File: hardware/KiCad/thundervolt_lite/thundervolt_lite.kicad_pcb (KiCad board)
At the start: 4 copper layers, 46.9 x 54.8 mm, 59 parts, among them U1 TPS628681ARQYR, U2 TPS628681ARQYR, U3 TPS628682ARQYR, U4 TPS63810YFFR, U5 ATTINY1616-MNR, U7 TMP1075NDRLR, U8 MIC5365-1.8YC5-TR

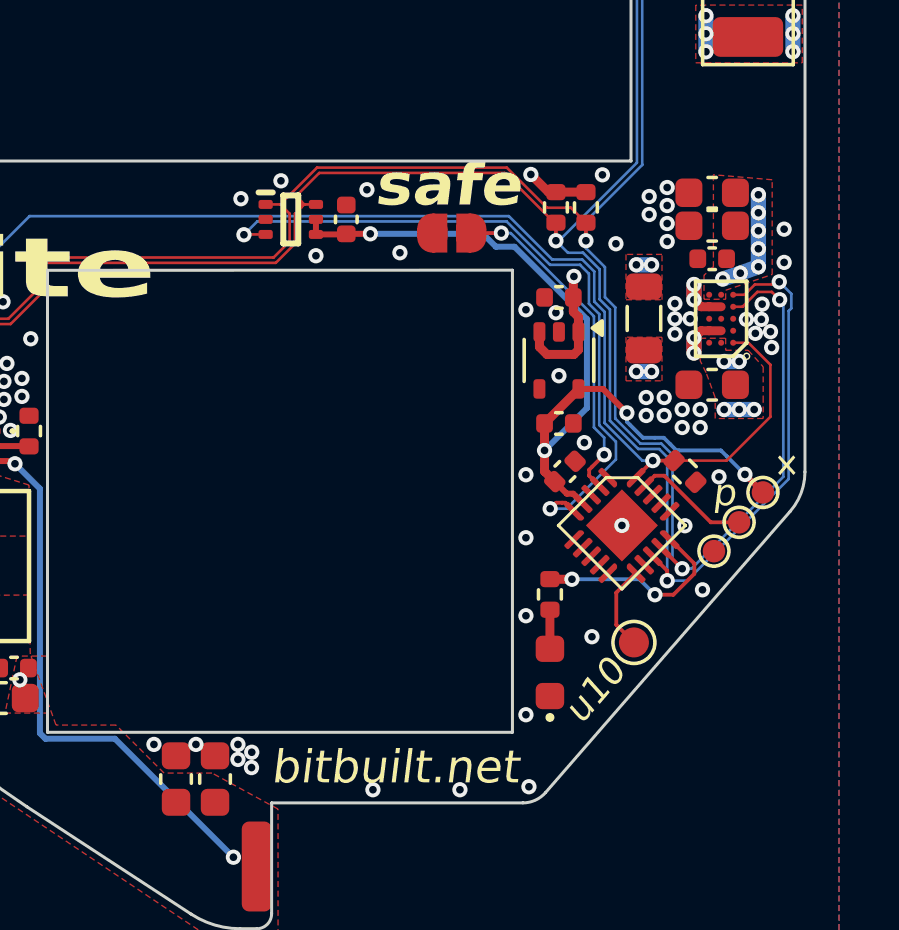
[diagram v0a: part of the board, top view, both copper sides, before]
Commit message: U10 FET Mode
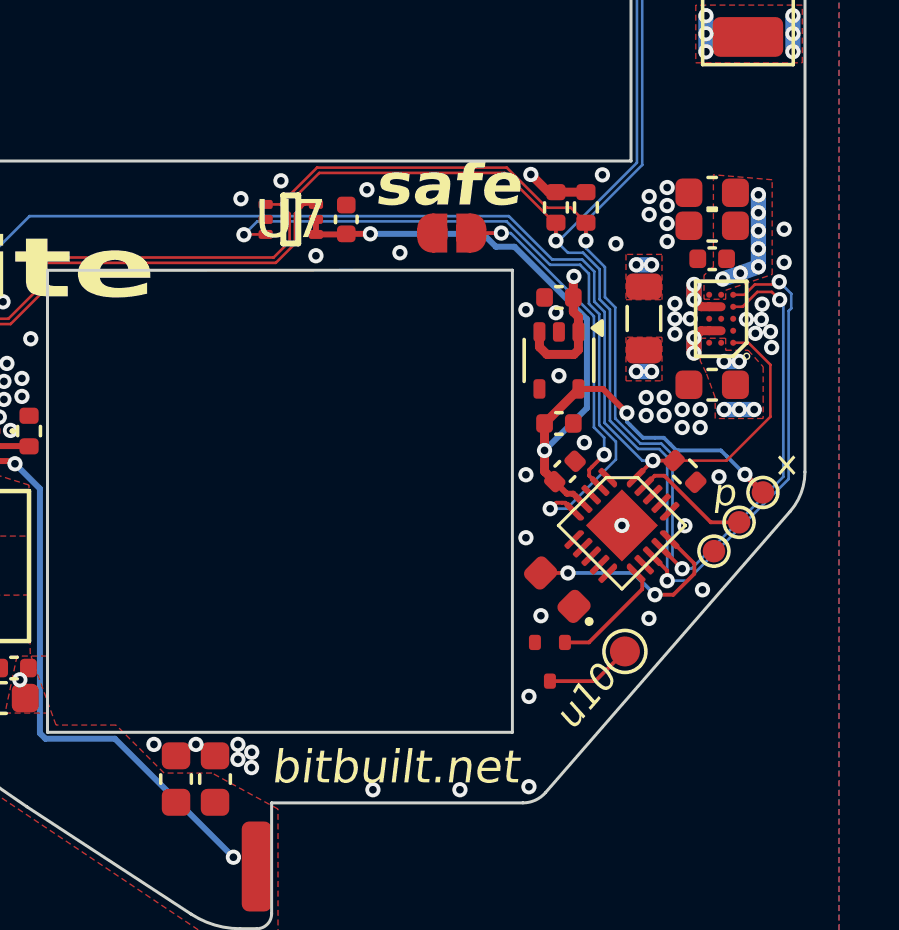
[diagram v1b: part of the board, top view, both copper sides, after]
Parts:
- removed R6: 0Ω, Resistor_SMD:R_0402_1005Metric
- added Q1: PJE8408_R1_00001, Package_TO_SOT_SMD:SOT-523, F.Cu at (156.9, 118.8)
- moved D1 2.77 mm to (157.2, 116.4), turned to 135 degrees
- moved TP6 0.42 mm to (159.4, 118.4)
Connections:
- U5 pad 11: U10 -> Net-(Q1-G)
- U5 pad 15: Net-(U5-PC0) -> Net-(D1-A)
- U5 pad 8: unconnected-(U5-PA7-Pad8) -> GND
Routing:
- net Net-(U5-PC0): track 6.82 -> 0.00 mm, vias 2 -> 0
- net Net-(D1-A): track 1.30 -> 7.21 mm, vias 0 -> 2
- net Net-(Q1-G): track 0.00 -> 3.94 mm
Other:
- copper layers 4 -> 13
